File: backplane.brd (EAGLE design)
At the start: 203.2 x 101.6 mm, 11 parts

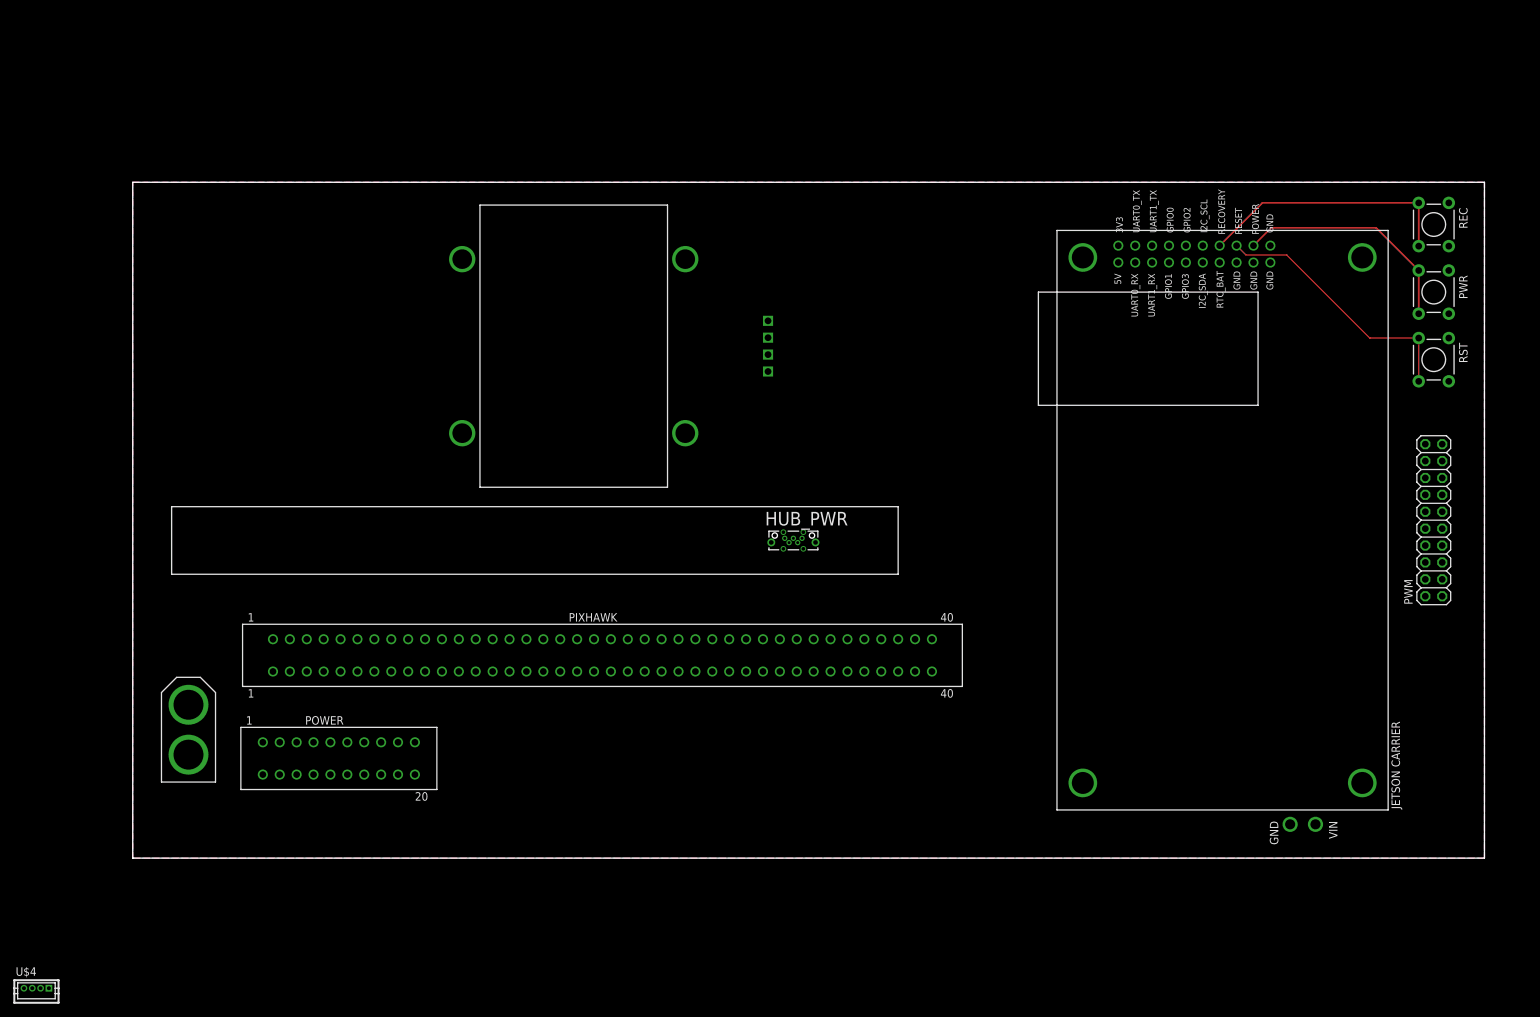
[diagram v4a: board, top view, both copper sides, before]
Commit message: Add pixhawk connectors
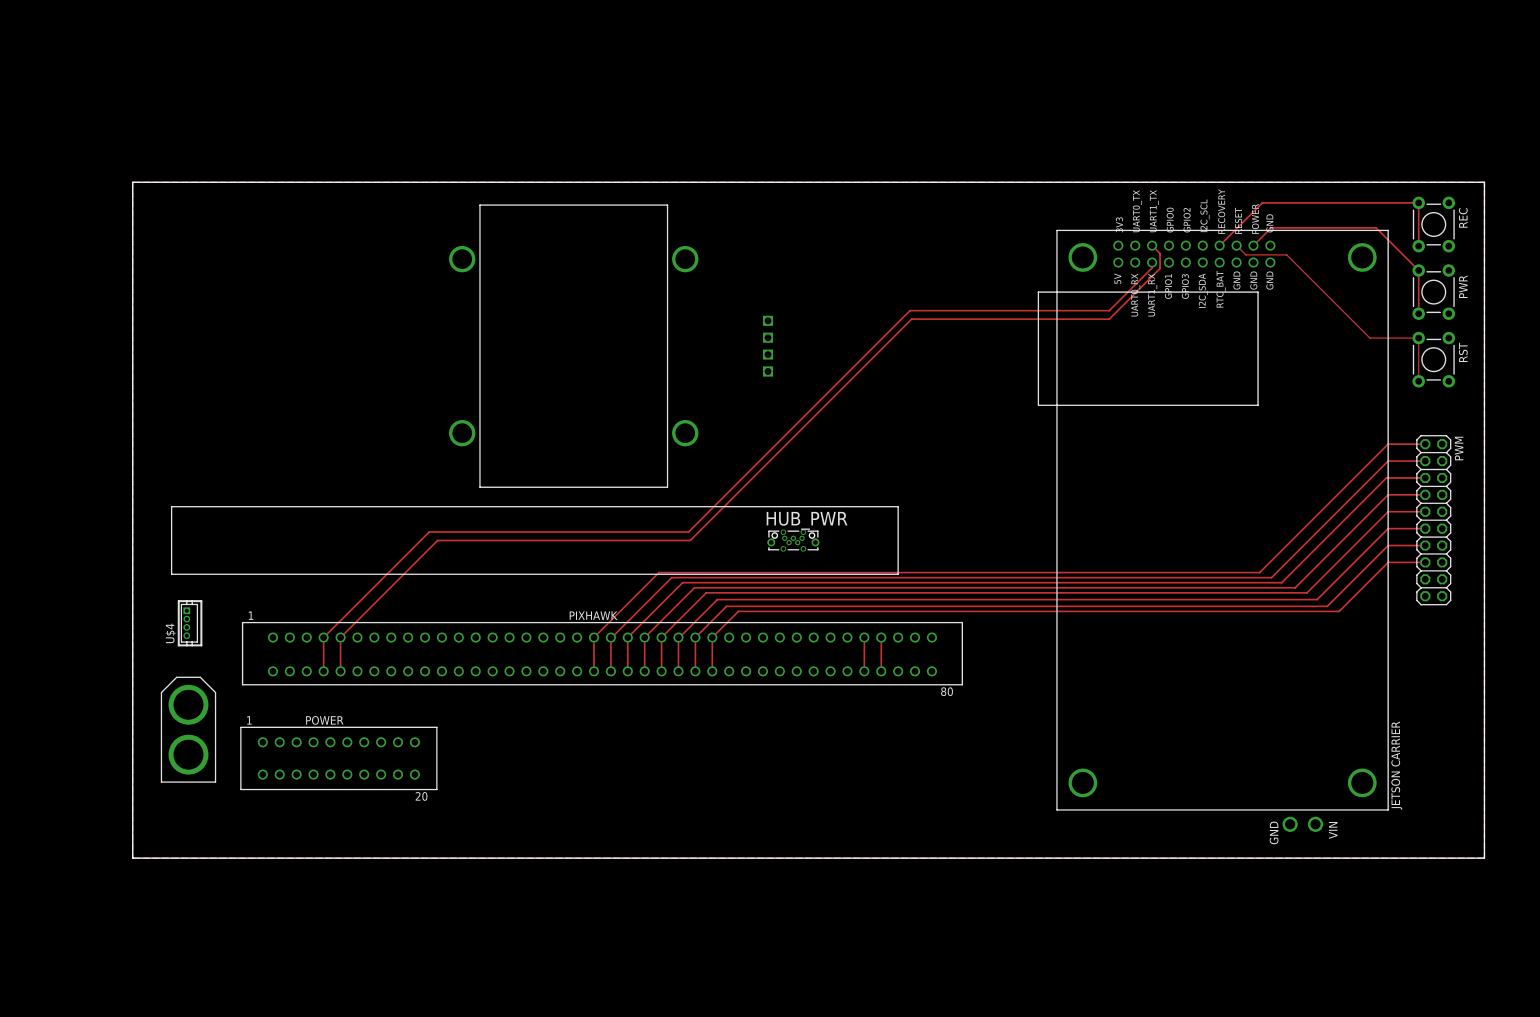
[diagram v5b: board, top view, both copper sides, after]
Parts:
- PIXHAWK: value TE-2-5530843-0 -> PIXHAWK_EDGE_CONNCONN
- moved U$4 59.3 mm to (8.13, 35.3), turned to 90 degrees
- moved PIXHAWK 0.25 mm to (70.6, 30.7)
- turned PWM to 270 degrees
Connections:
- removed net PIXHAWK_SCL: U$4.P$2
- removed net PIXHAWK_SDA: U$4.P$3
- new net N$1: PIXHAWK.39, PIXHAWK.40, PWM.1
- new net N$10: PIXHAWK.51, PIXHAWK.52, PWM.13
- new net N$11: PIXHAWK.53, PIXHAWK.54, PWM.15
- new net N$2: PIXHAWK.41, PIXHAWK.42, PWM.3
- new net N$6: PIXHAWK.43, PIXHAWK.44, PWM.5
- new net N$7: PIXHAWK.45, PIXHAWK.46, PWM.7
- new net N$8: PIXHAWK.47, PIXHAWK.48, PWM.9
- new net N$9: PIXHAWK.49, PIXHAWK.50, PWM.11
- new net PIXHAWK_I2C_SCL: PIXHAWK.71, PIXHAWK.72, U$4.P$2
- new net PIXHAWK_I2C_SDA: PIXHAWK.73, PIXHAWK.74, U$4.P$3
- net +5V: now also PIXHAWK.1, PIXHAWK.2, PIXHAWK.3, PIXHAWK.4, PIXHAWK.5, PIXHAWK.6
- net GND: now also PIXHAWK.75, PIXHAWK.76, PIXHAWK.77, PIXHAWK.78, PIXHAWK.79, PIXHAWK.80, PWM.10, PWM.12, PWM.14, PWM.16, PWM.18, PWM.2, PWM.20, PWM.4, PWM.6, PWM.8; no longer PWM.1, PWM.11, PWM.13, PWM.15, PWM.17, PWM.19, PWM.3, PWM.5, PWM.7, PWM.9
- net PIXHAWK_TELEM2_RX: now also PIXHAWK.10, PIXHAWK.9
- net PIXHAWK_TELEM2_TX: now also PIXHAWK.7, PIXHAWK.8
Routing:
- net PIXHAWK_TELEM2_RX: track 0.00 -> 155.2 mm
- net PIXHAWK_TELEM2_TX: track 0.00 -> 153.4 mm
- net N$1: track 0.00 -> 142.1 mm
- net N$2: track 0.00 -> 138.6 mm
- net N$6: track 0.00 -> 134.9 mm
- net N$7: track 0.00 -> 131.3 mm
- net N$8: track 0.00 -> 127.7 mm
- net N$9: track 0.00 -> 124.2 mm
- net N$10: track 0.00 -> 120.5 mm
- net N$11: track 0.00 -> 116.9 mm
- net PIXHAWK_I2C_SDA: track 0.00 -> 5.08 mm
- net PIXHAWK_I2C_SCL: track 0.00 -> 5.08 mm

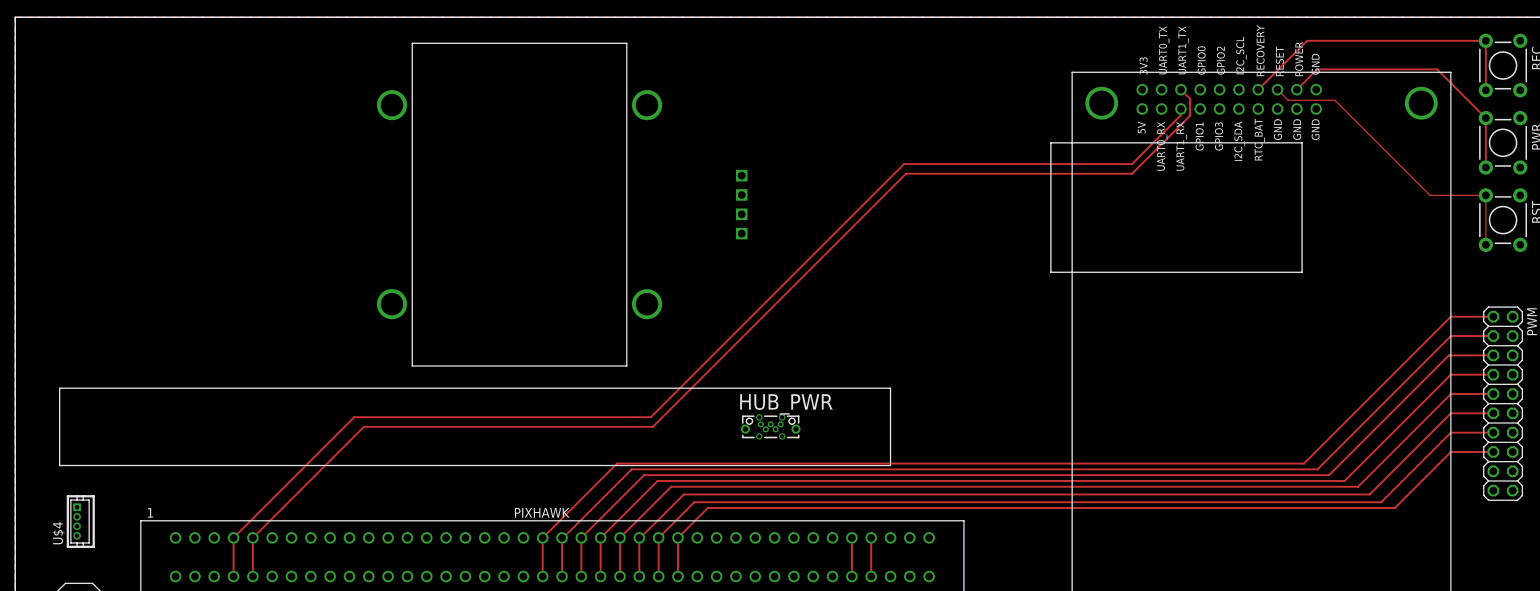
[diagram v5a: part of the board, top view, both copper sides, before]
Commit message: Add RS232-UART converter
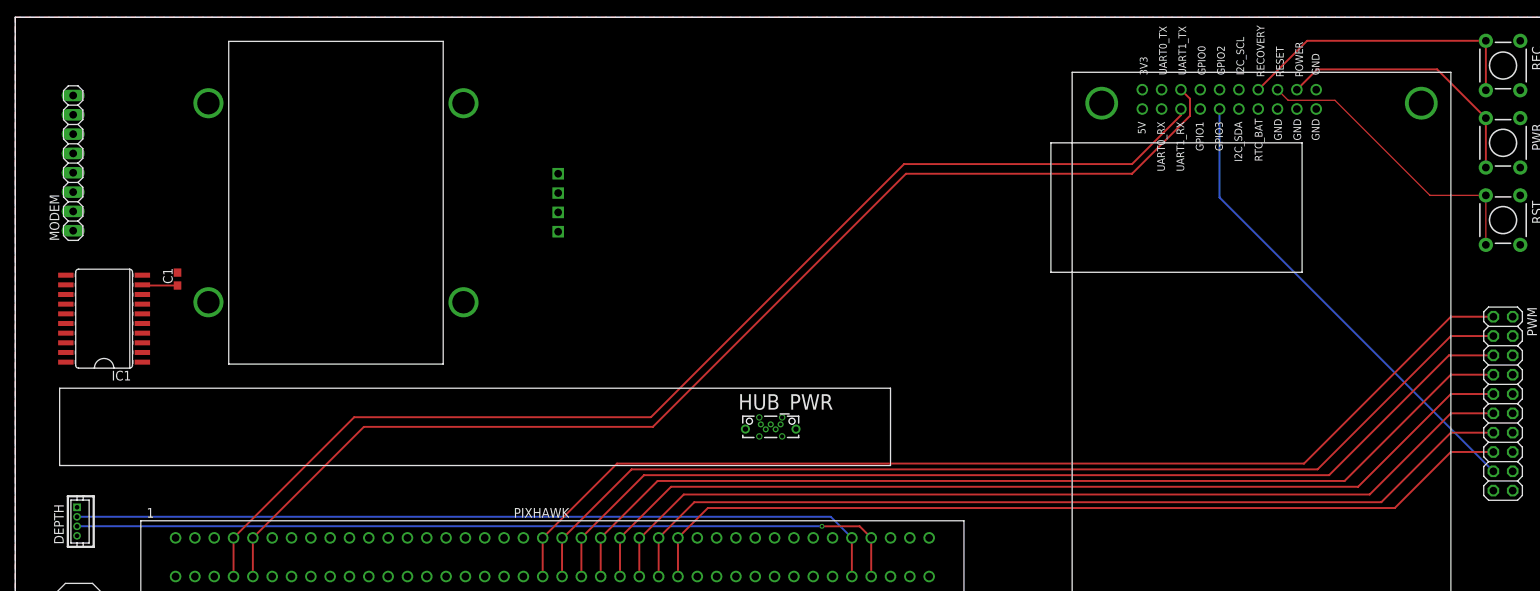
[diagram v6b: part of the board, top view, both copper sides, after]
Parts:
- added C1: (no value), auv:C0603
- added IC1: MAX3233ECWP, auv:SO20L
- added MODEM: (no value), auv:1X08
- moved U$1 24.1 mm to (42.2, 77.2)
- renumbered U$2 to BAT, U$4 to DEPTH
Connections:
- net N$1 renamed PWM1
- net N$10 renamed PWM7
- net N$11 renamed PWM8
- net N$2 renamed PWM2
- net N$6 renamed PWM3
- net N$7 renamed PWM4
- net N$8 renamed PWM5
- net N$9 renamed PWM6
- new net +3V3: C1.1, IC1.9
- new net MODEM_RS232_RX: IC1.8
- new net MODEM_RS232_TX: IC1.7
- new net MODEM_RX: IC1.6
- new net MODEM_TX: IC1.4
- new net PIXHAWK_GPIO3: PWM.17, U$3.GPIO3
- net GND: now also C1.2, IC1.18
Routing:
- net PIXHAWK_I2C_SDA: track 5.08 -> 110.1 mm, vias 0 -> 1
- net PIXHAWK_I2C_SCL: track 5.08 -> 108.1 mm
- net PIXHAWK_GPIO3: track 0.00 -> 62.5 mm
- net +3V3: track 0.00 -> 4.66 mm
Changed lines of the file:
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@@
 <setting verticaltext="up"/>
 </settings>
-<grid distance="10" unitdist="mil" unit="mil" style="lines" multiple="1" display="no" altdistance="5" altunitdist="mil" altunit="mil"/>
+<grid distance="5" unitdist="mil" unit="mil" style="lines" multiple="1" display="no" altdistance="5" altunitdist="mil" altunit="mil"/>
 <layers>
 <layer number="1" name="Top" color="4" fill="1" visible="yes" active="yes"/>
@@
 </element>
 <element name="PWM" library="auv" package="2X10" value="" x="195.58" y="50.8" rot="R270"/>
-<element name="U$1" library="auv" package="AHRS8P" value="AHRS8P" x="66.294" y="76.962" rot="R90"/>
+<element name="U$1" library="auv" package="AHRS8P" value="AHRS8P" x="42.164" y="77.216" rot="R90"/>
 <element name="POWER" library="auv" package="TE-5-5530843-0" value="TE-5-5530843-0" x="30.988" y="14.986"/>
-<element name="U$2" library="auv" package="XT-60" value="XT-60" x="8.382" y="19.304" rot="R270"/>
-<element name="U$4" library="auv" package="DF13-4P-1.25DSA" value="DF13-4P-1.25DSA" x="8.128" y="35.306" rot="R90"/>
+<element name="BAT" library="auv" package="XT-60" value="XT-60" x="8.382" y="19.304" rot="R270"/>
+<element name="DEPTH" library="auv" package="DF13-4P-1.25DSA" value="DF13-4P-1.25DSA" x="8.128" y="35.306" smashed="yes" rot="R90">
+<attribute name="NAME" x="6.38" y="32.308" size="1.27" layer="25" rot="R90"/>
+</element>
 <element name="PIXHAWK" library="auv" package="TE-2-5530843-0" value="PIXHAWK_EDGE_CONNCONN" x="70.612" y="30.734"/>
+<element name="MODEM" library="auv" package="1X08" value="" x="7.62" y="82.423" rot="R90"/>
+<element name="IC1" library="auv" package="SO20L" value="MAX3233ECWP" x="11.684" y="61.976" rot="R90">
+<attribute name="MF" value="MAXIM" x="11.684" y="61.976" size="1.778" layer="27" rot="R90" display="off"/>
+<attribute name="MPN" value="MAX3233ECWP" x="11.684" y="61.976" size="1.778" layer="27" rot="R90" display="off"/>
+<attribute name="OC_FARNELL" value="unknown" x="11.684" y="61.976" size="1.778" layer="27" rot="R90" display="off"/>
+<attribute name="OC_NEWARK" value="77C9167" x="11.684" y="61.976" size="1.778" layer="27" rot="R90" display="off"/>
+</element>
+<element name="C1" library="auv" package="C0603" value="" x="21.336" y="67.183" rot="R90"/>
 </elements>
 <signals>
@@
 </polygon>
 <contactref element="U$1" pad="GND"/>
-<contactref element="U$2" pad="P$2"/>
-<contactref element="U$4" pad="P$4"/>
+<contactref element="BAT" pad="P$2"/>
+<contactref element="DEPTH" pad="P$4"/>
 <contactref element="PWM" pad="2"/>
 <contactref element="PWM" pad="4"/>
@@
 <contactref element="PIXHAWK" pad="80"/>
 <contactref element="PIXHAWK" pad="78"/>
+<contactref element="IC1" pad="18"/>
+<contactref element="C1" pad="2"/>
+<wire x1="6.6548" y1="58.801" x2="21.336" y2="68.033" width="0" layer="19" extent="1-1"/>
+<wire x1="8.128" y1="33.431" x2="6.6548" y2="58.801" width="0" layer="19" extent="1-1"/>
 </signal>
 <signal name="VBAT">
@@
 <vertex x="0" y="0"/>
 </polygon>
-<contactref element="U$2" pad="P$1"/>
+<contactref element="BAT" pad="P$1"/>
 </signal>
 <signal name="PIXHAWK_TELEM2_TX">
@@
 <contactref element="PIXHAWK" pad="1"/>
 <contactref element="PIXHAWK" pad="4"/>
-<wire x1="98.014" y1="48.077" x2="95.504" y2="80.772" width="0" layer="19" extent="1-1"/>
-<wire x1="26.162" y1="33.1597" x2="98.014" y2="48.077" width="0" layer="19" extent="1-1"/>
+<wire x1="98.014" y1="48.077" x2="71.374" y2="81.026" width="0" layer="19" extent="1-1"/>
+<wire x1="26.162" y1="33.1597" x2="71.374" y2="81.026" width="0" layer="19" extent="1-1"/>
 <wire x1="23.622" y1="33.1597" x2="26.162" y2="33.1597" width="0" layer="19" extent="1-1"/>
 <wire x1="21.082" y1="33.1597" x2="23.622" y2="33.1597" width="0" layer="19" extent="1-1"/>
@@
 </signal>
 <signal name="5V">
-<contactref element="U$4" pad="P$1"/>
-</signal>
-<signal name="N$1">
+<contactref element="DEPTH" pad="P$1"/>
+</signal>
+<signal name="PWM1">
 <contactref element="PIXHAWK" pad="40"/>
 <contactref element="PIXHAWK" pad="39"/>
@@
 <wire x1="79.1083" y1="42.926" x2="169.418" y2="42.926" width="0.254" layer="1"/>
 </signal>
-<signal name="N$2">
+<signal name="PWM2">
 <contactref element="PWM" pad="3"/>
 <contactref element="PIXHAWK" pad="41"/>
@@
 <wire x1="171.196" y1="42.164" x2="81.026" y2="42.164" width="0.254" layer="1"/>
 </signal>
-<signal name="N$6">
+<signal name="PWM3">
 <contactref element="PIXHAWK" pad="44"/>
 <contactref element="PIXHAWK" pad="43"/>
@@
 <wire x1="82.6643" y1="41.402" x2="172.72" y2="41.402" width="0.254" layer="1"/>
 </signal>
-<signal name="N$7">
+<signal name="PWM4">
 <contactref element="PWM" pad="7"/>
 <contactref element="PIXHAWK" pad="45"/>
@@
 <wire x1="174.752" y1="40.64" x2="84.4423" y2="40.64" width="0.254" layer="1"/>
 </signal>
-<signal name="N$8">
+<signal name="PWM5">
 <contactref element="PIXHAWK" pad="47"/>
 <contactref element="PIXHAWK" pad="48"/>
@@
 <wire x1="86.2203" y1="39.878" x2="176.53" y2="39.878" width="0.254" layer="1"/>
 </signal>
-<signal name="N$9">
+<signal name="PWM6">
 <contactref element="PWM" pad="11"/>
 <contactref element="PIXHAWK" pad="50"/>
@@
 <wire x1="87.884" y1="38.862" x2="82.042" y2="33.02" width="0.254" layer="1"/>
 </signal>
-<signal name="N$10">
+<signal name="PWM7">
 <contactref element="PIXHAWK" pad="51"/>
 <contactref element="PIXHAWK" pad="52"/>
@@
 <wire x1="89.2683" y1="37.846" x2="179.578" y2="37.846" width="0.254" layer="1"/>
 </signal>
-<signal name="N$11">
+<signal name="PWM8">
 <contactref element="PWM" pad="15"/>
 <contactref element="PIXHAWK" pad="53"/>
@@
 <contactref element="PIXHAWK" pad="73"/>
 <contactref element="PIXHAWK" pad="74"/>
-<contactref element="U$4" pad="P$3"/>
+<contactref element="DEPTH" pad="P$3"/>
 <wire x1="112.522" y1="28.0797" x2="112.522" y2="33.1597" width="0.254" layer="1"/>
-<wire x1="8.128" y1="34.681" x2="112.522" y2="33.1597" width="0" layer="19" extent="1-1"/>
+<wire x1="8.128" y1="34.681" x2="106.055" y2="34.681" width="0.254" layer="16"/>
+<via x="106.055" y="34.681" extent="1-16" drill="0.35"/>
+<wire x1="106.055" y1="34.681" x2="111.0007" y2="34.681" width="0.254" layer="1"/>
+<wire x1="111.0007" y1="34.681" x2="112.522" y2="33.1597" width="0.254" layer="1"/>
 </signal>
 <signal name="PIXHAWK_I2C_SCL">
 <contactref element="PIXHAWK" pad="72"/>
 <contactref element="PIXHAWK" pad="71"/>
-<contactref element="U$4" pad="P$2"/>
+<contactref element="DEPTH" pad="P$2"/>
 <wire x1="109.982" y1="33.1597" x2="109.982" y2="28.0797" width="0.254" layer="1"/>
-<wire x1="8.128" y1="35.931" x2="109.982" y2="33.1597" width="0" layer="19" extent="1-1"/>
+<wire x1="8.128" y1="35.931" x2="107.2107" y2="35.931" width="0.254" layer="16"/>
+<wire x1="107.2107" y1="35.931" x2="109.982" y2="33.1597" width="0.254" layer="16"/>
+</signal>
+<signal name="PIXHAWK_GPIO3">
+<contactref element="U$3" pad="GPIO3"/>
+<contactref element="PWM" pad="17"/>
+<wire x1="194.31" y1="41.91" x2="158.3182" y2="77.9018" width="0.254" layer="16"/>
+<wire x1="158.3182" y1="77.9018" x2="158.3182" y2="89.535" width="0.254" layer="16"/>
+</signal>
+<signal name="MODEM_RS232_TX">
+<contactref element="IC1" pad="7"/>
+</signal>
+<signal name="MODEM_RS232_RX">
+<contactref element="IC1" pad="8"/>
+</signal>
+<signal name="MODEM_TX">
+<contactref element="IC1" pad="4"/>
+</signal>
+<signal name="MODEM_RX">
+<contactref element="IC1" pad="6"/>
+</signal>
+<signal name="+3V3">
+<contactref element="IC1" pad="9"/>
+<contactref element="C1" pad="1"/>
+<wire x1="21.336" y1="66.333" x2="16.8012" y2="66.333" width="0.254" layer="1"/>
+<wire x1="16.8012" y1="66.333" x2="16.7132" y2="66.421" width="0.254" layer="1"/>
 </signal>
 </signals>
